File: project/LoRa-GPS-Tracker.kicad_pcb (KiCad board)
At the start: 2 copper layers, 38.9 x 40 mm, 58 parts, among them IC1 MCP73831-2-OT, IC103 FT230XS, IC104 NCP705MT30TCG, IC2 MCP100-300D, M1 SIM28ML, M102 RAK3172, Q101 BSS123, Q102 TP0610K, Q103 BSH205G2VL, SW101 ON / OFF, X1 USB_B_Micro, X103 +, X104 -, X105 DEBUG, X3 Conn_Coaxial

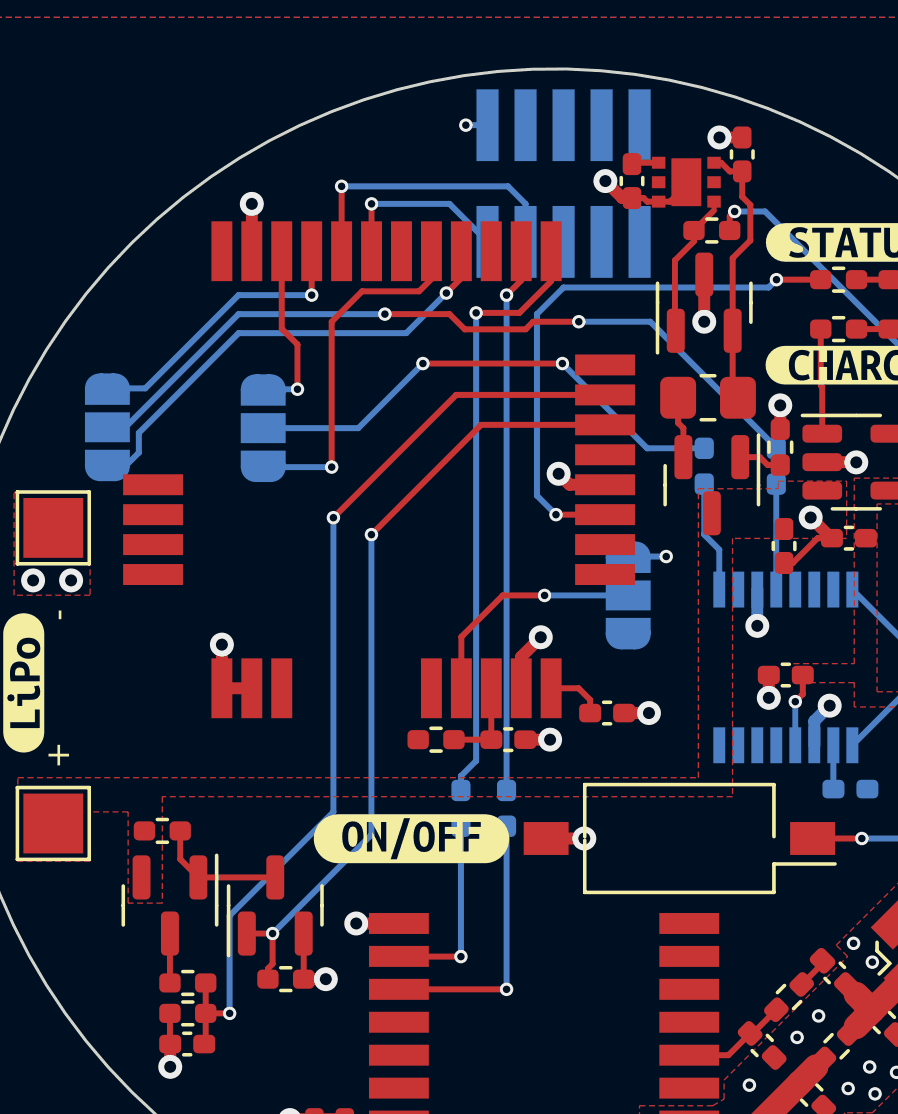
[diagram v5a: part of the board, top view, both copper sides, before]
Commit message: Working on version 1
Hardware:
- Finalize PCB
- Replace expensive components with cheaper ones
- Add GPS antenna

Firmware Testing:
- Add GPS configuration
- Add STOP mode sleep

Signed-off-by: Daniel Kampert <DanielKampert@kampis-elektroecke.de>
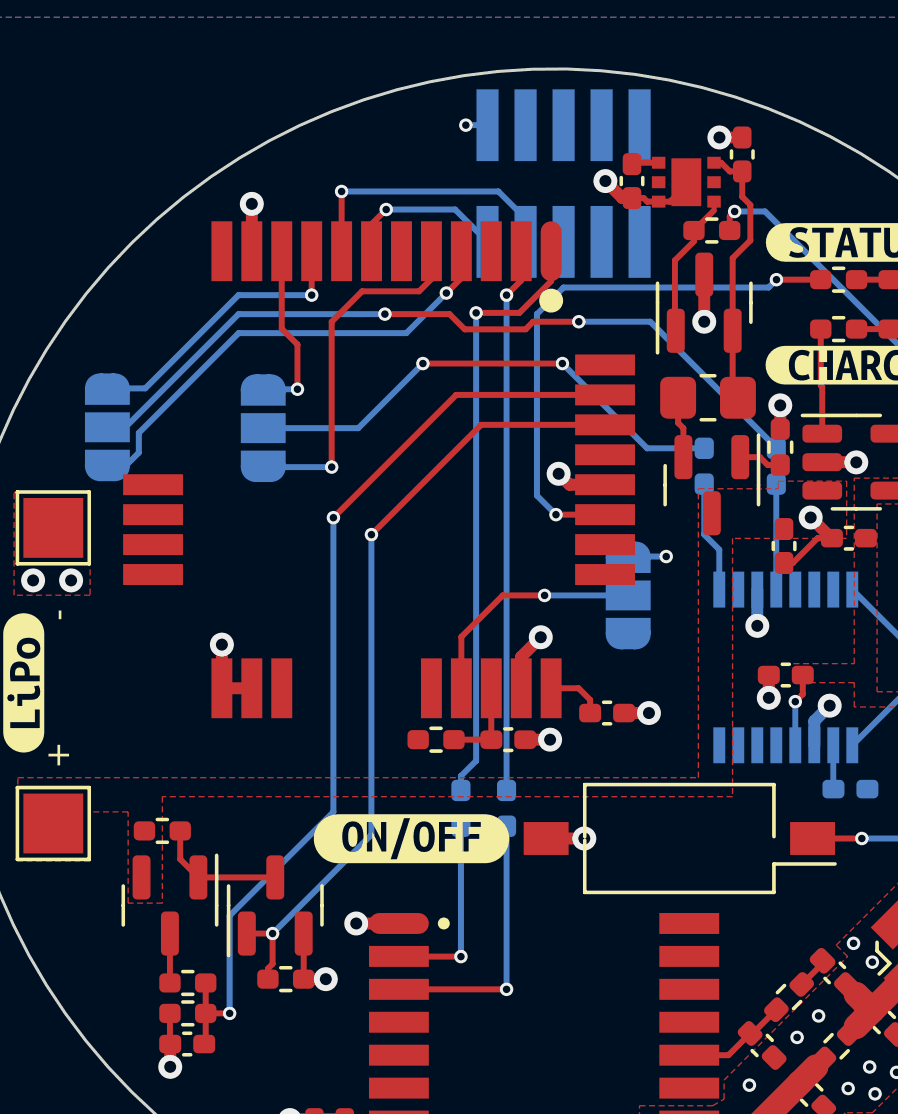
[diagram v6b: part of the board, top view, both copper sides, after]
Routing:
- net /SWDIO: track 5.98 -> 5.43 mm
- net /SWDCLK: track 9.83 -> 9.29 mm
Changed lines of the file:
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@@
         (effects (font (size 1 1) (thickness 0.15)))
     )
+    (fp_circle (center -3.35 -4.4) (end -3.25 -4.4)
+      (stroke (width 0.2) (type default)) (fill none) (layer "F.SilkS"))
     (fp_line (start -4.85 5.05) (end -4.85 -4.05)
       (stroke (width 0.1) (type solid)) (layer "F.Fab"))
@@
     (fp_line (start 4.85 5.05) (end -4.85 5.05)
       (stroke (width 0.1) (type solid)) (layer "F.Fab"))
-    (pad "1" smd rect (at -4.85 -4.4) (size 2 0.7) (layers "F.Cu" "F.Paste" "F.Mask")
+    (pad "1" smd oval (at -4.85 -4.4) (size 2 0.7) (layers "F.Cu" "F.Paste" "F.Mask")
       (net 1 "GND") (pinfunction "GND") (pintype "power_in"))
     (pad "2" smd rect (at -4.85 -3.3) (size 2 0.7) (layers "F.Cu" "F.Paste" "F.Mask")
@@
         (effects (font (size 1 1) (thickness 0.15)))
     )
+    (fp_circle (center -5.65 -5.75) (end -5.45 -5.75)
+      (stroke (width 0.4) (type default)) (fill none) (layer "F.SilkS"))
     (fp_line (start -7.5 -7.75) (end 7.5 -7.75)
       (stroke (width 0.05) (type default)) (layer "F.CrtYd"))
@@
     (fp_line (start 7.5 7.75) (end -7.5 7.75)
       (stroke (width 0.12) (type solid)) (layer "F.Fab"))
-    (pad "1" smd rect (at -7.3 -5.75 270) (size 2 0.7) (layers "F.Cu" "F.Paste" "F.Mask")
+    (pad "1" smd oval (at -7.3 -5.75 270) (size 2 0.7) (layers "F.Cu" "F.Paste" "F.Mask")
       (net 6 "/Tx_GNSS") (pinfunction "RX2") (pintype "input"))
     (pad "2" smd rect (at -7.3 -4.75 270) (size 2 0.7) (layers "F.Cu" "F.Paste" "F.Mask")
@@
   (segment (start 142.895571 116.951) (end 142.895571 111.5015) (width 0.2) (layer "B.Cu") (net 31))
   (segment (start 152.754787 116.787721) (end 153.454115 116.088392) (width 0.2) (layer "F.Cu") (net 35))
-  (segment (start 138.385571 90.711) (end 138.385571 92.293) (width 0.2) (layer "F.Cu") (net 47))
-  (via (at 138.385571 90.711) (size 0.45) (drill 0.25) (layers "F.Cu" "B.Cu") (net 47))
-  (segment (start 138.385571 90.711) (end 140.990571 90.711) (width 0.2) (layer "B.Cu") (net 47))
-  (segment (start 140.990571 90.711) (end 142.260571 91.981) (width 0.2) (layer "B.Cu") (net 47))
-  (segment (start 137.385571 90.125) (end 137.385571 92.293) (width 0.2) (layer "F.Cu") (net 48))
-  (via (at 137.385571 90.125) (size 0.45) (drill 0.25) (layers "F.Cu" "B.Cu") (net 48))
-  (segment (start 137.385571 90.125) (end 142.944571 90.125) (width 0.2) (layer "B.Cu") (net 48))
-  (segment (start 142.944571 90.125) (end 143.530571 90.711) (width 0.2) (layer "B.Cu") (net 48))
-  (segment (start 143.530571 90.711) (end 143.530571 91.981) (width 0.2) (layer "B.Cu") (net 48))
+  (segment (start 138.874877 90.899549) (end 138.385571 91.388855) (width 0.2) (layer "F.Cu") (net 47))
+  (segment (start 138.385571 91.388855) (end 138.385571 92.293) (width 0.2) (layer "F.Cu") (net 47))
+  (via (at 138.874877 90.899549) (size 0.45) (drill 0.25) (layers "F.Cu" "B.Cu") (net 47))
+  (segment (start 138.874877 90.899549) (end 141.17912 90.899549) (width 0.2) (layer "B.Cu") (net 47))
+  (segment (start 141.17912 90.899549) (end 142.260571 91.981) (width 0.2) (layer "B.Cu") (net 47))
+  (segment (start 137.385571 90.297) (end 137.385571 92.293) (width 0.2) (layer "F.Cu") (net 48))
+  (via (at 137.385571 90.297) (size 0.45) (drill 0.25) (layers "F.Cu" "B.Cu") (net 48))
+  (segment (start 143.530571 91.204571) (end 143.530571 91.981) (width 0.2) (layer "B.Cu") (net 48))
+  (segment (start 142.623 90.297) (end 143.530571 91.204571) (width 0.2) (layer "B.Cu") (net 48))
+  (segment (start 137.385571 90.297) (end 142.623 90.297) (width 0.2) (layer "B.Cu") (net 48))
   (segment (start 140.885522 93.690135) (end 141.385571 93.190086) (width 0.2) (layer "F.Cu") (net 49))
   (segment (start 141.385571 93.190086) (end 141.385571 92.293) (width 0.2) (layer "F.Cu") (net 49))

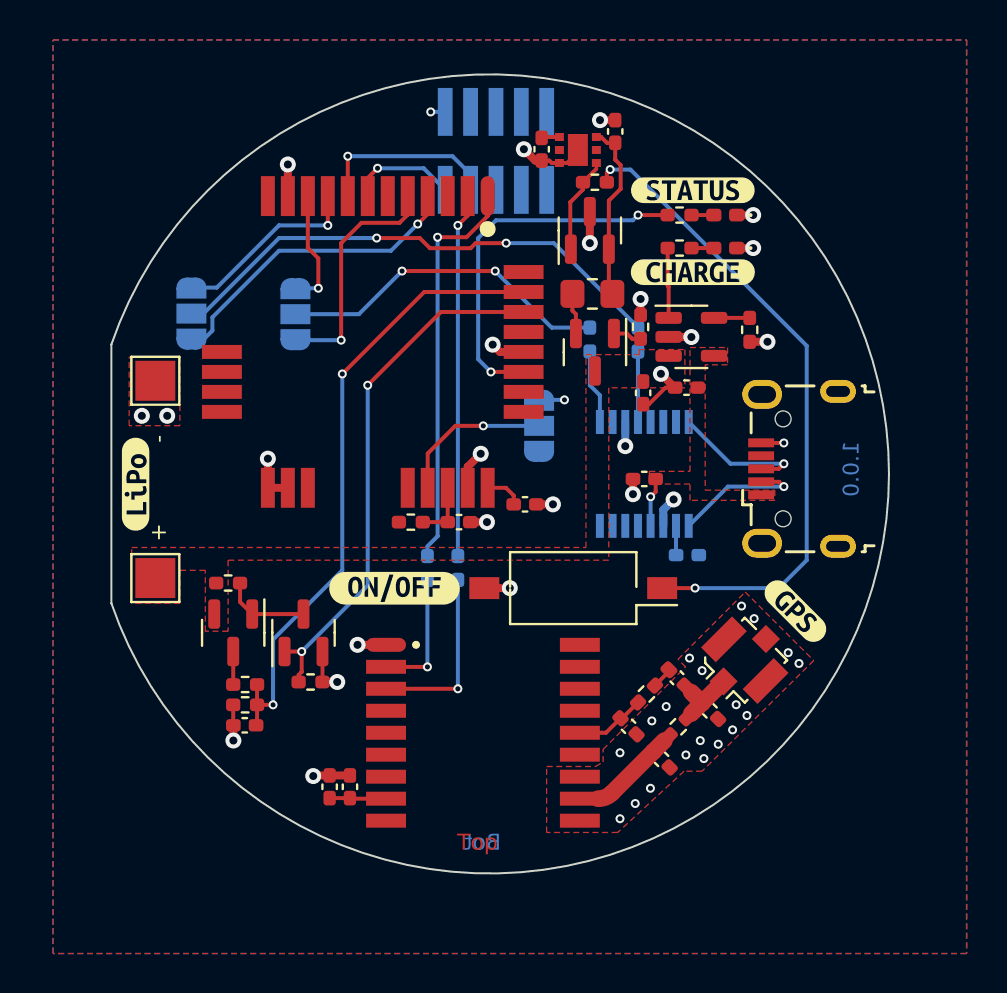
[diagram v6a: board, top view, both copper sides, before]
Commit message: Hardware: - Add RESET line for SWD interface - Replace micro USB with USB C
Software:
- Add firmware for LoRa-GPS-Tracker PCB

Signed-off-by: Daniel Kampert <DanielKampert@kampis-elektroecke.de>
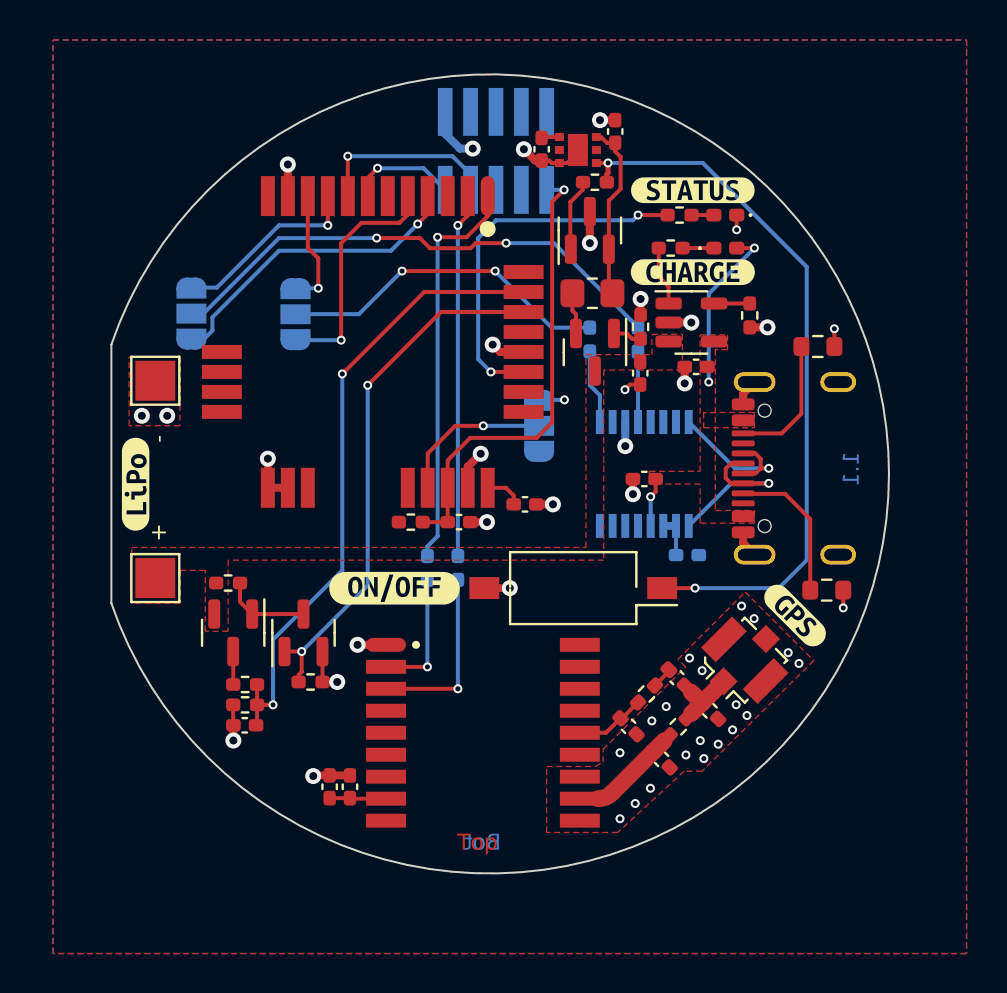
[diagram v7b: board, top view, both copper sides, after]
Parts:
- removed X1: USB_B_Micro, Wuerth:629105150521
- added R107: 5k1, Resistor_SMD:R_0603_1608Metric, F.Cu at (161.4, 112.0)
- added R108: 5k1, Resistor_SMD:R_0603_1608Metric, F.Cu at (160.9, 99.8)
- added X101: DEBUG, Connector_USB:USB_C_Receptacle_GCT_USB4105-xx-A_16P_TopMnt_Horizontal, F.Cu at (160.9, 105.9)
- JP101: value ~ -> RX
- JP102: value ~ -> TX
- JP103: value PROG -> BOOT
- R111: renamed from R107; value 2k -> 10k
- moved C105 1.15 mm to (154.8, 100.8)
- moved C109 0.99 mm to (152.0, 101.2)
- moved IC1 0.72 mm to (154.6, 98.6)
- moved R111 0.72 mm to (157.5, 98.3)
- moved R112 0.45 mm to (153.5, 94.9)
- moved kibuzzard-65A18804 0.22 mm to (159.8, 113.3)
- turned D101 to 0 degrees
- turned R115 to 180 degrees
- renumbered C105 to C104, C104 to C105, C109 to C108, C108 to C109, R103 to R101, R101 to R102, R102 to R103, R108 to R109, R109 to R110, R110 to R112, R111 to R113, R112 to R114, R113 to R115, R114 to R116, R115 to R117, R116 to R118, R117 to R119
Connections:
- C113 pad 1: Net-(M102-~{RST}) -> /~{RESET}
- D101 pad 1: GND -> Net-(D101-K)
- D101 pad 2: Net-(D101-A) -> /V_USB
- IC103 pad 11: +3V0 -> Net-(IC103-3V3OUT)
- IC104 pad 4: Net-(IC102-~{RST}) -> Net-(IC104-EN)
- M102 pad 22: Net-(M102-~{RST}) -> /~{RESET}
- R112 pad 2: Net-(D101-A) -> Net-(D101-K)
- R115 pad 1: Net-(IC102-~{RST}) -> Net-(IC104-EN)
- R115 pad 2: Net-(R113-Pad2) -> Net-(IC102-~{RST})
- R118 pad 2: Net-(M102-~{RST}) -> /~{RESET}
- SW101 pad 1: Net-(R113-Pad2) -> Net-(IC104-EN)
- X105 pad 10: unconnected-(X105-~{RESET}-Pad10) -> /~{RESET}
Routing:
- net Net-(IC104-EN): track 0.00 -> 36.2 mm, vias 0 -> 2
- net Net-(R113-Pad2): track 32.7 -> 0.00 mm, vias 2 -> 0
- net /~{RESET}: track 0.00 -> 23.1 mm, vias 0 -> 1
- net /V_USB: track 2.45 -> 11.0 mm, vias 1 -> 3
- net Net-(X101-CC1): track 0.00 -> 7.45 mm
- net Net-(X101-CC2): track 0.00 -> 6.69 mm
- net Net-(M102-~{RST}): track 2.97 -> 0.00 mm
- net /USB_DM: track 6.81 -> 8.61 mm
- net Net-(D101-K): track 0.00 -> 1.56 mm
- net GND: track 32.9 -> 34.2 mm, vias 43 -> 44
- net Net-(D101-A): track 1.12 -> 0.00 mm
- net Net-(IC102-~{RST}): track 4.74 -> 3.63 mm
- net /USB_DP: track 6.87 -> 7.83 mm
- net Net-(IC103-3V3OUT): track 1.47 -> 2.10 mm
- net Net-(IC101-STAT): track 3.52 -> 2.98 mm
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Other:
- board text added: "1.${REVISION}"
- board text removed: "1.0.0"

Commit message: - Upgrade KiBot to support KiCad 8
Signed-off-by: Daniel Kampert <DanielKampert@kampis-elektroecke.de>
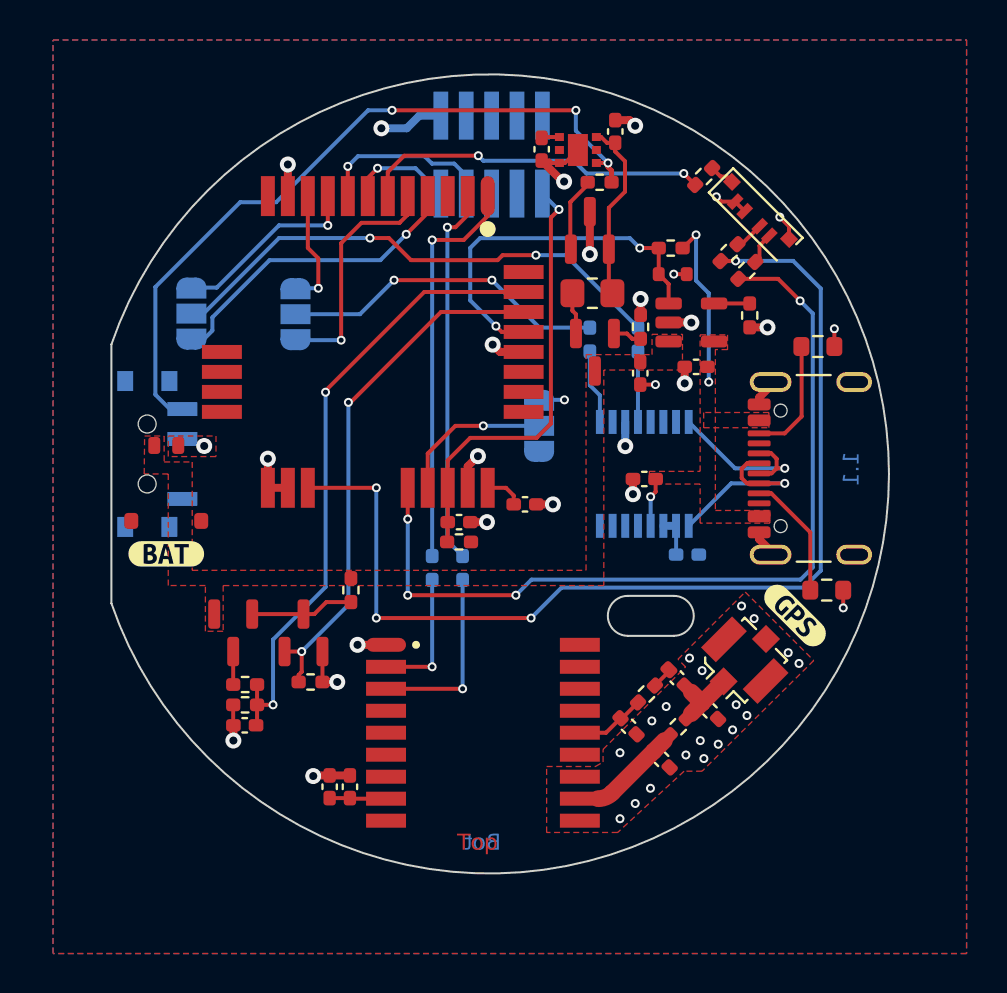
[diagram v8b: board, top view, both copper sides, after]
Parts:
- removed D102: STATUS, LED_SMD:LED_0402_1005Metric_Pad0.77x0.64mm_HandSolder
- removed SW101: ON / OFF, Button_Switch_SMD:SW_DIP_SPSTx01_Slide_Omron_A6S-110x_W8.9mm_P2.54mm
- removed the X104 at (127.8, 101.5)
- removed kibuzzard-65985972: G***, kibuzzard-65985972
- removed kibuzzard-65985988: G***, kibuzzard-65985988
- removed kibuzzard-659DAEA0: G***, kibuzzard-659DAEA0
- removed kibuzzard-65A18838: G***, kibuzzard-65A18838
- added D103: CLS6B-FKW, Cree:QLS6B-FKW-CNSNSF043, F.Cu at (157.8, 93.2)
- added R120: 120R, Resistor_SMD:R_0402_1005Metric_Pad0.72x0.64mm_HandSolder, F.Cu at (156.5, 95.1)
- added R121: 240R, Resistor_SMD:R_0402_1005Metric_Pad0.72x0.64mm_HandSolder, F.Cu at (155.2, 91.3)
- added SW102: ON/OFF, Button_Switch_SMD:SW_SPDT_PCM12, B.Cu at (127.7, 105.2)
- added kibuzzard-66008FCD: G***, kibuzzard-66008FCD, F.Cu at (128.3, 110.2)
- D101: value CHARGE -> D_Zener; footprint LED_SMD:LED_0402_1005Metric_Pad0.77x0.64mm_HandSolder -> Diode_SMD:D_SOD-523
- R112: value 270R -> 1k
- R119: value 270R -> 120R
- X103: value + -> BATTERY; footprint TestPoint:TestPoint_Pad_2.0x2.0mm -> Molex:78171-0002
- moved R104 6.16 mm to (137.5, 112.0), turned to -90 degrees
- moved X103 4.79 mm to (128.3, 106.7), turned to 0 degrees
- moved R119 4.36 mm to (157.4, 96.0), turned to 45 degrees
- moved D101 2.94 mm to (153.6, 96.2)
- moved R118 2.61 mm to (143.0, 109.6), turned to 180 degrees
- moved X101 0.80 mm to (161.7, 105.9)
- moved X104 0.29 mm to (144.6, 90.2)
- moved R102 0.24 mm to (141.6, 110.9)
- moved R103 0.24 mm to (143.1, 110.9)
- moved R115 0.24 mm to (150.0, 91.6)
- renumbered IC1 to IC101, IC2 to IC102, L1 to L101, M1 to M101, X3 to X102, X105 to X104
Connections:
- D101 pad 1: Net-(D101-K) -> /CHARGE
- D101 pad 2: /V_USB -> GND
- IC101 pad 1: Net-(IC101-STAT) -> /CHARGE
- M102 pad 19: unconnected-(M102-PA8-Pad19) -> Net-(M102-PA8)
- M102 pad 20: unconnected-(M102-PA9-Pad20) -> Net-(M102-PA9)
- M102 pad 27: Net-(M102-PB12) -> unconnected-(M102-PB12-Pad27)
- M102 pad 29: unconnected-(M102-PA0-Pad29) -> /CHARGE
- M102 pad 6: unconnected-(M102-PA1-Pad6) -> Net-(M102-PA1)
- R112 pad 1: Net-(IC101-STAT) -> /CHARGE
- R112 pad 2: Net-(D101-K) -> /V_USB
- R119 pad 1: Net-(M102-PB12) -> Net-(M102-PA9)
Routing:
- net Net-(M102-PA8): track 0.00 -> 52.9 mm, vias 0 -> 4
- net Net-(M102-PA9): track 0.00 -> 43.4 mm, vias 0 -> 4
- net /CHARGE: track 0.00 -> 18.8 mm, vias 0 -> 2
- net Net-(M102-PB12): track 18.6 -> 0.00 mm, vias 2 -> 0
- net Net-(M102-PA1): track 0.00 -> 17.5 mm, vias 0 -> 2
- net Net-(IC101-STAT): track 2.98 -> 0.00 mm
- net GND: track 34.2 -> 37.0 mm
- net Net-(D101-K): track 1.56 -> 0.00 mm
- net Net-(D103-AG): track 0.00 -> 1.48 mm
- net Net-(D103-AR): track 0.00 -> 1.28 mm
- net Net-(X101-CC1): track 7.45 -> 6.26 mm
- net /~{RESET}: track 23.1 -> 22.1 mm
- net Net-(IC104-EN): track 36.2 -> 37.1 mm, vias 2 -> 3
- net Net-(X101-CC2): track 6.69 -> 5.78 mm
- net Net-(Q101-D): track 4.37 -> 5.19 mm
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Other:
- outline, holes or cut-outs redrawn
